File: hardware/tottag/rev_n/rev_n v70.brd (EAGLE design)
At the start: 68.1 x 36.9 mm, 197 parts, among them J1 TC2030-JLINK-NL-2SIDE, J2 TC2030-JLINK-NL-2SIDE, J4 MOLEX-PICO-SPOX-3SIDE, Q1 CSD75207W15, Q2 MOSFET-NCHANNELXFDN-3, U1 APOLLO4_BLUE_PLUS_SOC_KBR, U2 DW3110, U3 BQ24040, U4 BQ51013B, U6 BNO086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

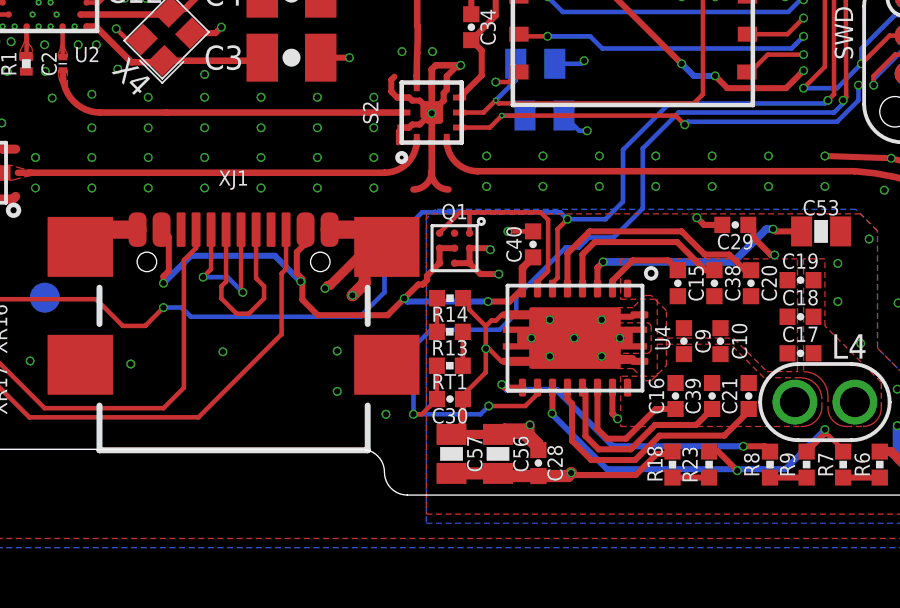
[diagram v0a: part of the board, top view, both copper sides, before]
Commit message: rev_n: Updates from DFM review
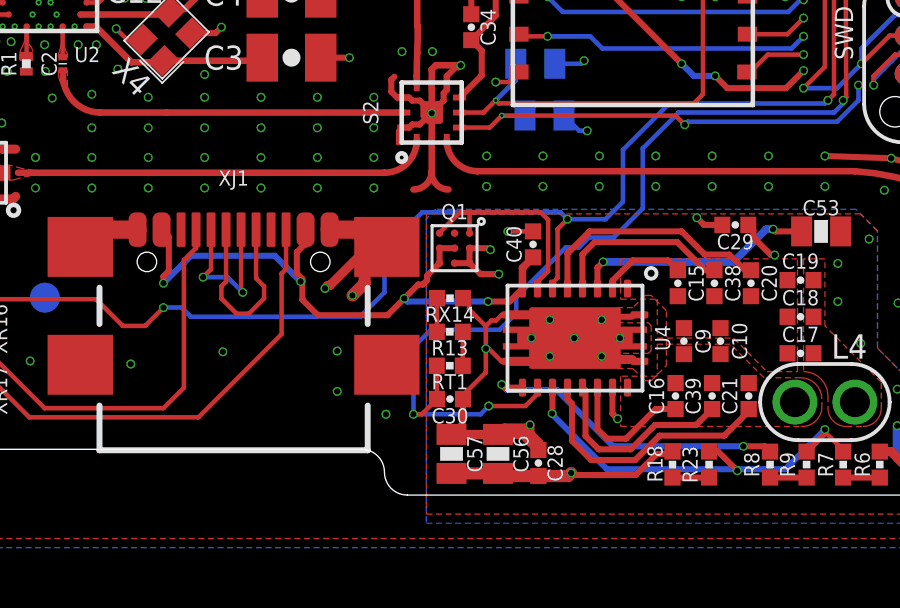
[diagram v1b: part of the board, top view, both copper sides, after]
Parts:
- R13: value 1k -> 2.2k
- RX14: value 1k -> DNP
- renumbered R14 to RX14
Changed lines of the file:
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@@
 <layer number="27" name="tValues" color="7" fill="1" visible="no" active="yes"/>
 <layer number="28" name="bValues" color="7" fill="1" visible="no" active="yes"/>
-<layer number="29" name="tStop" color="7" fill="3" visible="yes" active="yes"/>
+<layer number="29" name="tStop" color="7" fill="3" visible="no" active="yes"/>
 <layer number="30" name="bStop" color="7" fill="6" visible="no" active="yes"/>
 <layer number="31" name="tCream" color="7" fill="4" visible="no" active="yes"/>
@@
 <class number="0" name="default" width="0" drill="0">
 </class>
-<class number="1" name="BLE_RF" width="0" drill="0">
+<class number="1" name="BLE_RF" width="0.22" drill="0">
+<clearance class="1" value="0.15"/>
 </class>
-<class number="2" name="UWB_RF" width="0" drill="0">
+<class number="2" name="UWB_RF" width="0.22" drill="0">
+<clearance class="2" value="0.15"/>
 </class>
-<class number="3" name="USB_PHY" width="0" drill="0">
+<class number="3" name="USB_PHY" width="0.1524" drill="0">
+<clearance class="3" value="0.3048"/>
 </class>
-<class number="4" name="UWB_XTAL" width="0" drill="0">
+<class number="4" name="UWB_XTAL" width="0.22" drill="0">
+<clearance class="4" value="0.15"/>
 </class>
 </classes>
-<designrules name="drc">
+<designrules name="drc *">
 <param name="mdWireWire" value="4mil"/>
 <param name="mdWirePad" value="4mil"/>
@@
 <param name="mvStopFrame" value="1"/>
 <param name="mvCreamFrame" value="0"/>
-<param name="mlMinStopFrame" value="4mil"/>
-<param name="mlMaxStopFrame" value="4mil"/>
+<param name="mlMinStopFrame" value="1mil"/>
+<param name="mlMaxStopFrame" value="1.25mil"/>
 <param name="mlMinCreamFrame" value="0mil"/>
 <param name="mlMaxCreamFrame" value="0mil"/>
-<param name="mlViaStopLimit" value="0mil"/>
+<param name="mlViaStopLimit" value="12mil"/>
 <param name="srRoundness" value="0"/>
 <param name="srMinRoundness" value="0mil"/>
@@
 </element>
 <element name="R15" library="passives" library_urn="urn:adsk.eagle:library:20904581" package="0402_RES" package3d_urn="urn:adsk.eagle:package:20904668/2" value="2.2k" x="-18.288" y="7.8232" smashed="yes" rot="R180">
-<attribute name="DIGIKEY" value="RMCF0402JT2K20CT-ND" x="-18.288" y="7.8232" size="1.778" layer="27" rot="R180" display="off"/>
-<attribute name="MPN" value="RMCF0402JT2K20" x="-18.288" y="7.8232" size="1.778" layer="27" rot="R180" display="off"/>
+<attribute name="MPN" value="RC0402FR-072K2L" x="-18.288" y="7.8232" size="1.778" layer="27" rot="R180" display="off"/>
 <attribute name="NAME" x="-18.288" y="7.5184" size="0.508" layer="25" font="vector" ratio="18" rot="R180" align="bottom-center"/>
 <attribute name="VALUE" x="-18.288" y="9.2202" size="0.508" layer="27" font="vector" ratio="18" rot="R180" align="bottom-center"/>
@@
 <attribute name="NAME" x="1.016" y="-3.556" size="0.508" layer="25" font="vector" ratio="18" rot="R180" align="bottom-center"/>
 </element>
-<element name="R13" library="passives" package="0402_RES" value="1k" x="1.01011875" y="-1.01011875" smashed="yes">
+<element name="R13" library="passives" package="0402_RES" value="2.2k" x="1.01011875" y="-1.01011875" smashed="yes">
+<attribute name="MPN" value="RC0402FR-072K2L" x="1.01011875" y="-1.01011875" size="1.778" layer="27" display="off"/>
 <attribute name="NAME" x="1.01011875" y="-1.28951875" size="0.508" layer="25" font="vector" ratio="18" rot="R180" align="bottom-center"/>
+<attribute name="TOL" value="1%" x="1.01011875" y="-1.01011875" size="1.778" layer="27" display="off"/>
 <attribute name="VALUE" x="1.01011875" y="-2.40711875" size="0.508" layer="27" font="vector" ratio="18" align="bottom-center"/>
 </element>
-<element name="R14" library="passives" package="0402_RES" value="1k" x="1.016" y="0.1104875" smashed="yes" rot="R180">
+<element name="RX14" library="passives" package="0402_RES" value="DNP" x="1.016" y="0.1104875" smashed="yes" rot="R180">
 <attribute name="NAME" x="1.016" y="-0.1689125" size="0.508" layer="25" font="vector" ratio="18" rot="R180" align="bottom-center"/>
 <attribute name="VALUE" x="1.016" y="1.5074875" size="0.508" layer="27" font="vector" ratio="18" rot="R180" align="bottom-center"/>
@@
 <contactref element="C29" pad="2"/>
 <contactref element="C30" pad="2"/>
-<contactref element="R14" pad="1"/>
+<contactref element="RX14" pad="1"/>
 <via x="-20.2946" y="-2.5146" extent="1-16" drill="0.2032">
 </via>
@@
 <signal name="N$70">
 <contactref element="R13" pad="1"/>
-<contactref element="R14" pad="2"/>
+<contactref element="RX14" pad="2"/>
 <wire x1="0.58293125" y1="0.1104875" x2="0.58293125" y2="-1.0042375" width="0.1524" layer="1"/>
 <wire x1="0.58293125" y1="-1.0042375" x2="0.57705" y2="-1.01011875" width="0.1524" layer="1"/>
